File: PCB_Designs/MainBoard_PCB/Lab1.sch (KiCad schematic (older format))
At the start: 84 parts, among them K1 XLR3, P1 CONN_01X06, P10 CONN_01X01, P11 CONN_01X01, P12 CONN_01X01, P2 USB_B, P3 CONN_02X05, P4 CONN_01X02, P5 CONN_02X05, P6 CONN_02X05, P7 CONN_01X01, P8 CONN_01X01, P9 CONN_01X01, Q1 BSS138, Q2 BSS138, Q3 BSS138, Q4 BSS138, Q5 BSS138, Q6 BSS138, Q7 BSS138, U1 STM32F411RETx, U10 24C16, U2 TRACO_POWER_TEL_2-0511, U3 6N137, U4 6N137, U5 6N137, U6 FT232RL, U7 MAX481CSA, U8 UA78M05IDCY, U9 UA78M33CDCY, Y1 8MHz

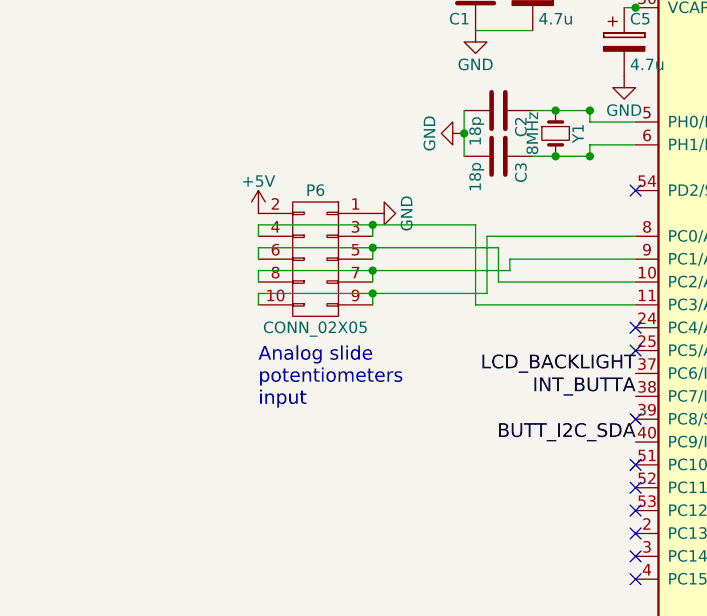
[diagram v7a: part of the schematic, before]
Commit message: Edited Main_PCB from feedback.
* Added RC-filter (1Mohm, 100nF)
Little cramped now, but whatever.
* Filled out groundplanes a little
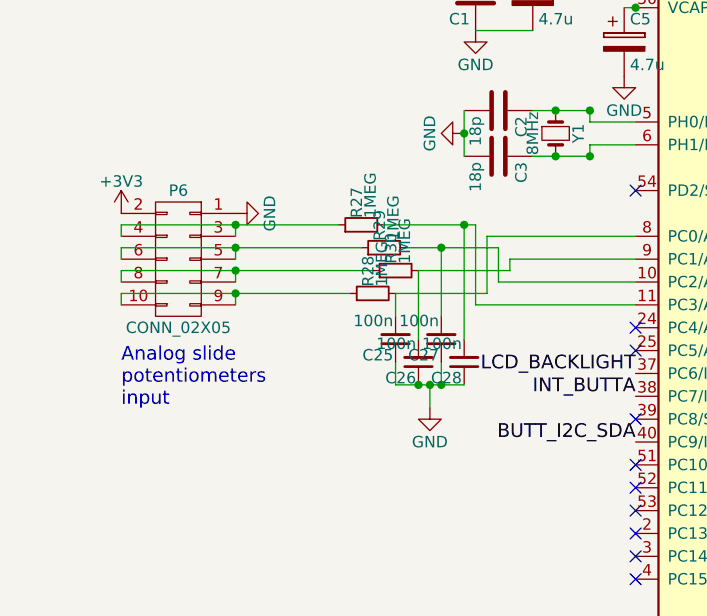
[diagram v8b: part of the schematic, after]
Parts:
- added C25, C26, C27, C28: 100n, Capacitors_SMD:C_0603_HandSoldering, symbol C_Small
- added R27, R28, R29, R30: 1MEG, Resistors_SMD:R_0603_HandSoldering, symbol R_Small
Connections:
- net +3V3: now also P6.2 (P2)
- net +5V: no longer P6.2 (P2)
- net GND: now also C25.1, C26.1, C27.1, C28.1
- net at P6.5 (P5), P6.6 (P6): now also R29.1; no longer U1.10 (PC2/ADC1_IN12/I2S2_ext_SD/SPI2_MISO)
- net at P6.3 (P3), P6.4 (P4): now also R27.1; no longer U1.11 (PC3/ADC1_IN13/I2S2_SD/SPI2_MOSI)
- net at P6.10 (P10), P6.9 (P9): now also R28.1; no longer U1.8 (PC0/ADC1_IN10)
- net at P6.7 (P7), P6.8 (P8): now also R30.1; no longer U1.9 (PC1/ADC1_IN11)
- new net: C27.2, R29.2, U1.10 (PC2/ADC1_IN12/I2S2_ext_SD/SPI2_MISO)
- new net: C28.2, R27.2, U1.11 (PC3/ADC1_IN13/I2S2_SD/SPI2_MOSI)
- new net: C25.2, R28.2, U1.8 (PC0/ADC1_IN10)
- new net: C26.2, R30.2, U1.9 (PC1/ADC1_IN11)
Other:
- moved on the sheet: P6
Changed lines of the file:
@@
 EESchema Schematic File Version 2
 LIBS:Lab1-rescue
+LIBS:lm1117
 LIBS:stm32f4
 LIBS:stm32f100
@@
 L CONN_02X05 P6
 U 1 1 58A11651
-P 1900 4150
-F 0 "P6" H 1900 4450 50  0000 C CNN
-F 1 "CONN_02X05" H 1900 3850 50  0000 C CNN
-F 2 "Connectors_Multicomp:Multicomp_MC9A22-1034_2x05x2.54mm_Angled" H 1900 2950 50  0001 C CNN
-F 3 "" H 1900 2950 50  0000 C CNN
-	1    1900 4150
+P 1300 4150
+F 0 "P6" H 1300 4450 50  0000 C CNN
+F 1 "CONN_02X05" H 1300 3850 50  0000 C CNN
+F 2 "Connectors_Multicomp:Multicomp_MC9A22-1034_2x05x2.54mm_Angled" H 1300 2950 50  0001 C CNN
+F 3 "" H 1300 2950 50  0000 C CNN
+	1    1300 4150
 	-1   0    0    -1
 $EndComp
@@
 L GND #PWR053
 U 1 1 58A11657
-P 2150 3950
-F 0 "#PWR053" H 2150 3700 50  0001 C CNN
-F 1 "GND" H 2150 3800 50  0000 C CNN
-F 2 "" H 2150 3950 50  0000 C CNN
-F 3 "" H 2150 3950 50  0000 C CNN
-	1    2150 3950
+P 1550 3950
+F 0 "#PWR053" H 1550 3700 50  0001 C CNN
+F 1 "GND" H 1550 3800 50  0000 C CNN
+F 2 "" H 1550 3950 50  0000 C CNN
+F 3 "" H 1550 3950 50  0000 C CNN
+	1    1550 3950
 	0    -1   1    0
-$EndComp
-$Comp
-L +5V #PWR054
-U 1 1 58A1165D
-P 1650 3950
-F 0 "#PWR054" H 1650 3800 50  0001 C CNN
-F 1 "+5V" H 1650 4090 50  0000 C CNN
-F 2 "" H 1650 3950 50  0000 C CNN
-F 3 "" H 1650 3950 50  0000 C CNN
-	1    1650 3950
-	-1   0    0    -1
 $EndComp
 $Comp
@@
 	1    0    0    -1
 $EndComp
-Text Notes 1650 4800 0    60   ~ 0
+Text Notes 1050 4800 0    60   ~ 0
 Analog slide \npotentiometers\ninput
 Text Notes 5300 7350 0    60   ~ 0
@@
 NoConn ~ 3300 4850
 Wire Wire Line
-	2150 4300 2150 4350
-Wire Wire Line
-	1650 4300 2650 4300
-Wire Wire Line
-	1650 4350 1650 4300
-Wire Wire Line
-	2150 4200 2150 4250
-Wire Wire Line
-	1650 4200 2750 4200
-Wire Wire Line
-	1650 4250 1650 4200
-Wire Wire Line
-	2150 4100 2150 4150
-Wire Wire Line
-	1650 4100 2700 4100
-Wire Wire Line
-	1650 4150 1650 4100
-Wire Wire Line
-	1650 4000 1650 4050
-Wire Wire Line
-	1650 4000 2600 4000
-Wire Wire Line
-	2150 4050 2150 4000
+	1550 4300 1550 4350
+Wire Wire Line
+	1050 4300 2050 4300
+Wire Wire Line
+	1050 4350 1050 4300
+Wire Wire Line
+	1550 4200 1550 4250
+Wire Wire Line
+	1050 4200 2150 4200
+Wire Wire Line
+	1050 4250 1050 4200
+Wire Wire Line
+	1550 4100 1550 4150
+Wire Wire Line
+	1050 4100 2100 4100
+Wire Wire Line
+	1050 4150 1050 4100
+Wire Wire Line
+	1050 4000 1050 4050
+Wire Wire Line
+	1050 4000 2000 4000
+Wire Wire Line
+	1550 4050 1550 4000
 Wire Wire Line
 	2450 6600 2450 6650
@@
 Wire Wire Line
 	2650 4050 3300 4050
-Connection ~ 2150 4300
+Connection ~ 1550 4300
 Wire Wire Line
 	2750 4200 2750 4150
 Wire Wire Line
 	2750 4150 3300 4150
-Connection ~ 2150 4200
+Connection ~ 1550 4200
 Wire Wire Line
 	2700 4100 2700 4250
 Wire Wire Line
 	2700 4250 3300 4250
-Connection ~ 2150 4100
+Connection ~ 1550 4100
 Wire Wire Line
 	2600 4000 2600 4350
 Wire Wire Line
 	2600 4350 3300 4350
-Connection ~ 2150 4000
+Connection ~ 1550 4000
 $Comp
 L C C21
@@
 NoConn ~ 8600 -950
 NoConn ~ 9300 -950
+$Comp
+L R_Small R27
+U 1 1 58A72FDA
+P 2100 4000
+F 0 "R27" H 2130 4020 50  0000 L CNN
+F 1 "1MEG" H 2130 3960 50  0000 L CNN
+F 2 "Resistors_SMD:R_0603_HandSoldering" H 2100 4000 50  0001 C CNN
+F 3 "" H 2100 4000 50  0001 C CNN
+	1    2100 4000
+	0    -1   -1   0
+$EndComp
+$Comp
+L R_Small R29
+U 1 1 58A87860
+P 2200 4100
+F 0 "R29" H 2230 4120 50  0000 L CNN
+F 1 "1MEG" H 2230 4060 50  0000 L CNN
+F 2 "Resistors_SMD:R_0603_HandSoldering" H 2200 4100 50  0001 C CNN
+F 3 "" H 2200 4100 50  0001 C CNN
+	1    2200 4100
+	0    -1   -1   0
+$EndComp
+$Comp
+L R_Small R30
+U 1 1 58A87976
+P 2250 4200
+F 0 "R30" H 2280 4220 50  0000 L CNN
+F 1 "1MEG" H 2280 4160 50  0000 L CNN
+F 2 "Resistors_SMD:R_0603_HandSoldering" H 2250 4200 50  0001 C CNN
+F 3 "" H 2250 4200 50  0001 C CNN
+	1    2250 4200
+	0    -1   -1   0
+$EndComp
+$Comp
+L R_Small R28
+U 1 1 58A87AE4
+P 2150 4300
+F 0 "R28" H 2180 4320 50  0000 L CNN
+F 1 "1MEG" H 2180 4260 50  0000 L CNN
+F 2 "Resistors_SMD:R_0603_HandSoldering" H 2150 4300 50  0001 C CNN
+F 3 "" H 2150 4300 50  0001 C CNN
+	1    2150 4300
+	0    -1   -1   0
+$EndComp
+Wire Wire Line
+	2200 4000 2600 4000
+Wire Wire Line
+	2300 4100 2700 4100
+Wire Wire Line
+	2350 4200 2750 4200
+Wire Wire Line
+	2250 4300 2650 4300
+$Comp
+L C_Small C25
+U 1 1 58A892E7
+P 2250 4500
+F 0 "C25" H 2260 4570 50  0000 L CNN
+F 1 "100n" H 2260 4420 50  0000 L CNN
+F 2 "Capacitors_SMD:C_0603_HandSoldering" H 2250 4500 50  0001 C CNN
+F 3 "" H 2250 4500 50  0001 C CNN
+	1    2250 4500
+	-1   0    0    1
+$EndComp
+$Comp
+L C_Small C26
+U 1 1 58A8954E
+P 2350 4600
+F 0 "C26" H 2360 4670 50  0000 L CNN
+F 1 "100n" H 2360 4520 50  0000 L CNN
+F 2 "Capacitors_SMD:C_0603_HandSoldering" H 2350 4600 50  0001 C CNN
+F 3 "" H 2350 4600 50  0001 C CNN
+	1    2350 4600
+	-1   0    0    1
+$EndComp
+$Comp
+L C_Small C27
+U 1 1 58A8967E
+P 2450 4500
+F 0 "C27" H 2460 4570 50  0000 L CNN
+F 1 "100n" H 2460 4420 50  0000 L CNN
+F 2 "Capacitors_SMD:C_0603_HandSoldering" H 2450 4500 50  0001 C CNN
+F 3 "" H 2450 4500 50  0001 C CNN
+	1    2450 4500
+	-1   0    0    1
+$EndComp
+$Comp
+L C_Small C28
+U 1 1 58A897A3
+P 2550 4600
+F 0 "C28" H 2560 4670 50  0000 L CNN
+F 1 "100n" H 2560 4520 50  0000 L CNN
+F 2 "Capacitors_SMD:C_0603_HandSoldering" H 2550 4600 50  0001 C CNN
+F 3 "" H 2550 4600 50  0001 C CNN
+	1    2550 4600
+	-1   0    0    1
+$EndComp
+$Comp
+L GND #PWR062
+U 1 1 58A8B0ED
+P 2400 4800
+F 0 "#PWR062" H 2400 4550 50  0001 C CNN
+F 1 "GND" H 2400 4650 50  0000 C CNN
+F 2 "" H 2400 4800 50  0001 C CNN
+F 3 "" H 2400 4800 50  0001 C CNN
+	1    2400 4800
+	1    0    0    -1
+$EndComp
+Wire Wire Line
+	2250 4700 2550 4700
+Wire Wire Line
+	2250 4600 2250 4700
+Connection ~ 2350 4700
+Wire Wire Line
+	2450 4600 2450 4700
+Connection ~ 2450 4700
+Wire Wire Line
+	2400 4700 2400 4800
+Connection ~ 2400 4700
+Wire Wire Line
+	2550 4500 2550 4000
+Connection ~ 2550 4000
+Wire Wire Line
+	2450 4400 2450 4100
+Connection ~ 2450 4100
+Wire Wire Line
+	2350 4500 2350 4200
+Wire Wire Line
+	2250 4400 2250 4300
+$Comp
+L +3V3 #PWR?
+U 1 1 58A8EA42
+P 1050 3950
+F 0 "#PWR?" H 1050 3800 50  0001 C CNN
+F 1 "+3V3" H 1050 4090 50  0000 C CNN
+F 2 "" H 1050 3950 50  0000 C CNN
+F 3 "" H 1050 3950 50  0000 C CNN
+	1    1050 3950
+	1    0    0    -1
+$EndComp
 $EndSCHEMATC
